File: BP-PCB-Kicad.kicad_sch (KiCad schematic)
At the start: 18 parts, among them J1 A3C-50DA-2DSA_71_, J13 Conn_01x20, J14 Conn_01x20, J15 DF14-30P-1.25H_35_, J16 A3C-50DA-2DSA_71_, J17 A3C-4DA-2DSA_71_, J18 A3C-4DA-2DSA_71_, J19 Molex 55460-0272, J2 A3C-50DA-2DSA_71_, J21 Molex 55460-0272, J22 Molex 55460-0272, J23 DF14-15P-1.25H52, J3 A3C-4DA-2DSA_71_, J4 A3C-4DA-2DSA_71_, J5 A3C-50DA-2DSA_71_, J6 A3C-50DA-2DSA_71_, J7 DF14-15P-1.25H52, J8 DF14-15P-1.25H52

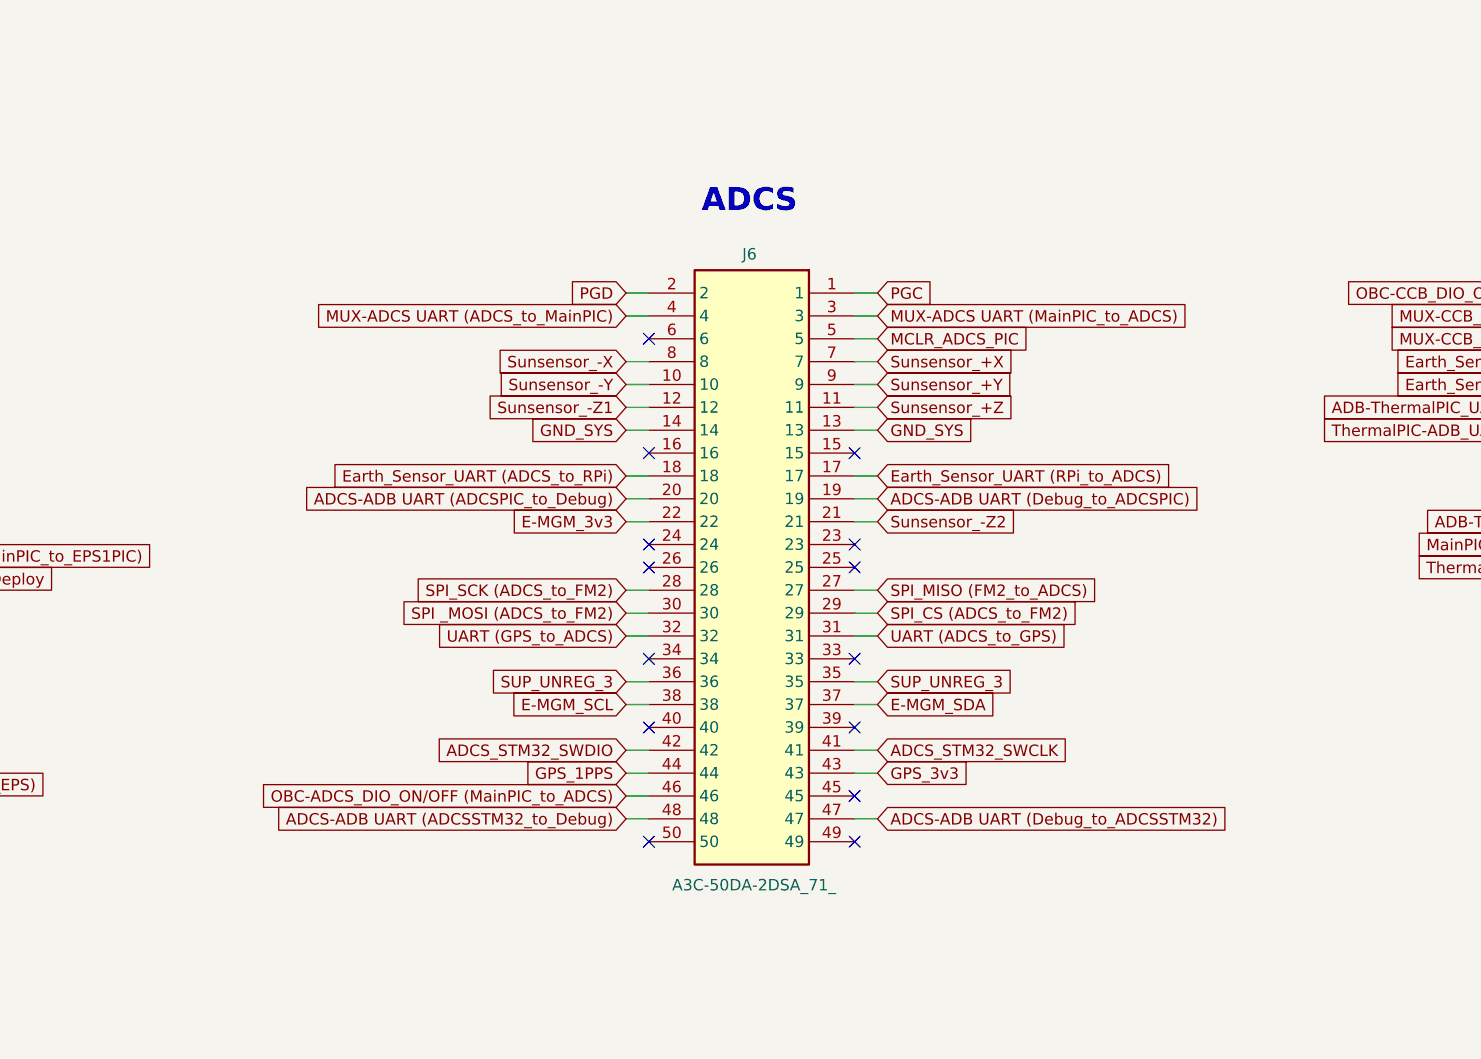
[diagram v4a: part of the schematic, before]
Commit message: Routing traces of panels
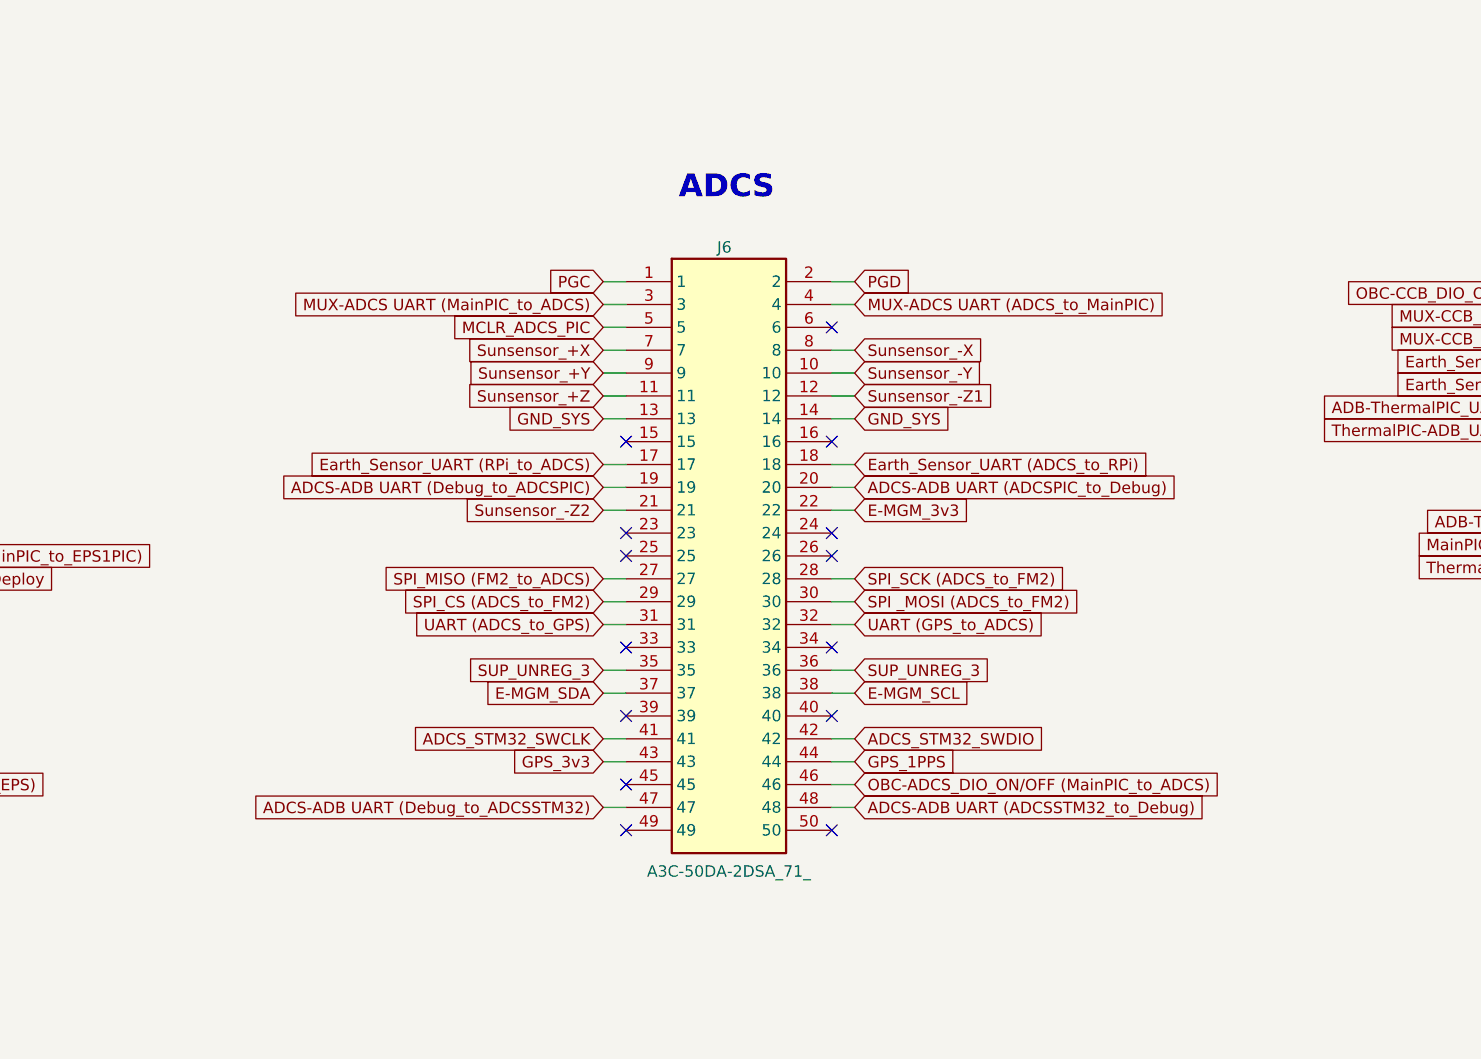
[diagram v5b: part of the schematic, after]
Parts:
- removed J6: A3C-50DA-2DSA_71_, Custom-Footprints:Hirose_A3C-50DA-2DSC(71)_Mirrored, symbol Custom-Symbols:A3C-50DA-2DSA_71_Mirrored
- added J6: A3C-50DA-2DSA_71_, Custom-Footprints:Hirose_A3C-50DA-2DSC(71), symbol Custom-Symbols:A3C-50DA-2DSA_71_
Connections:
- net ADCS-ADB UART (ADCSPIC_to_Debug): now also J6.20
- net ADCS-ADB UART (ADCSSTM32_to_Debug): now also J6.48
- net ADCS-ADB UART (Debug_to_ADCSPIC): now also J6.19
- net ADCS-ADB UART (Debug_to_ADCSSTM32): now also J6.47
- net ADCS_STM32_SWCLK: now also J6.41
- net ADCS_STM32_SWDIO: now also J6.42
- net E-MGM_3v3: now also J6.22
- net E-MGM_SCL: now also J6.38
- net E-MGM_SDA: now also J6.37
- net Earth_Sensor_UART (ADCS_to_RPi): now also J6.18
- net Earth_Sensor_UART (RPi_to_ADCS): now also J6.17
- net GND_SYS: now also J6.13, J6.14
- net GPS_1PPS: now also J6.44
- net GPS_3v3: now also J6.43
- net MCLR_ADCS_PIC: now also J6.5
- net MUX-ADCS UART (ADCS_to_MainPIC): now also J6.4
- net MUX-ADCS UART (MainPIC_to_ADCS): now also J6.3
- net OBC-ADCS_DIO_ON/OFF (MainPIC_to_ADCS): now also J6.46
- net PGC: now also J6.1
- net PGD: now also J6.2
- net SPI _MOSI (ADCS_to_FM2): now also J6.30
- net SPI_CS (ADCS_to_FM2): now also J6.29
- net SPI_MISO (FM2_to_ADCS): now also J6.27
- net SPI_SCK (ADCS_to_FM2): now also J6.28
- net SUP_UNREG_3: now also J6.35, J6.36
- net Sunsensor_+X: now also J6.7
- net Sunsensor_+Y: now also J6.9
- net Sunsensor_+Z: now also J6.11
- net Sunsensor_-X: now also J6.8
- net Sunsensor_-Y: now also J6.10
- net Sunsensor_-Z1: now also J6.12
- net Sunsensor_-Z2: now also J6.21
- net UART (ADCS_to_GPS): now also J6.31
- net UART (GPS_to_ADCS): now also J6.32

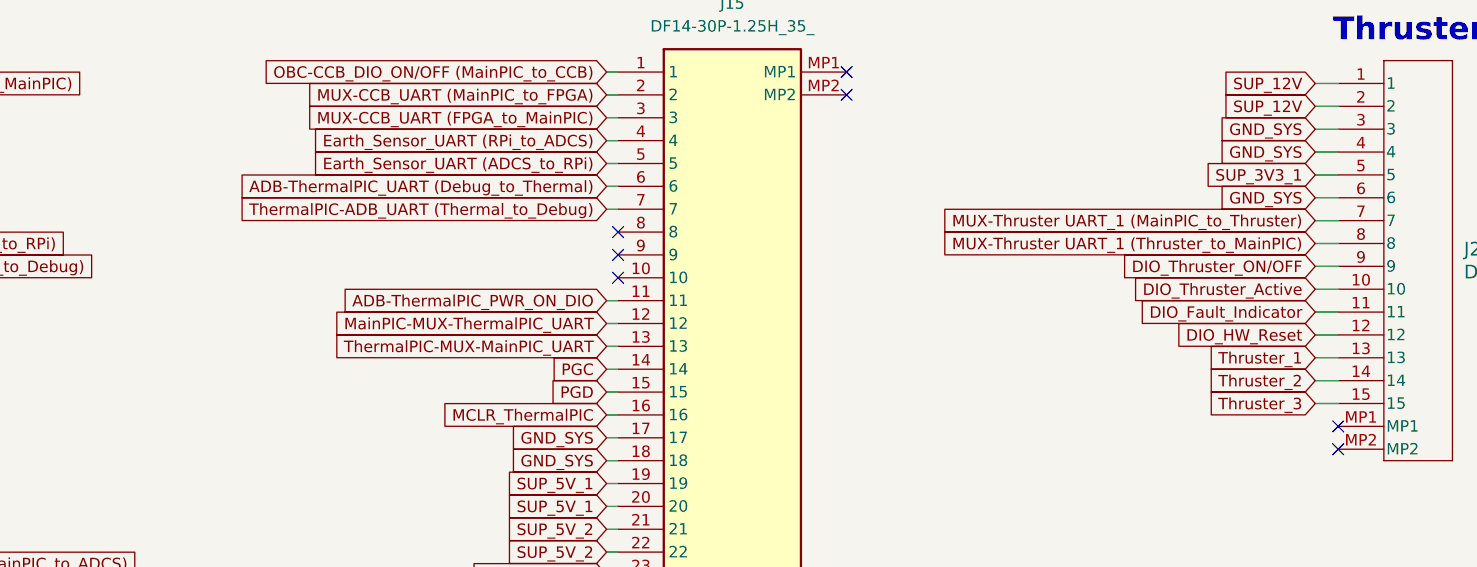
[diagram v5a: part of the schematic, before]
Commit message: Corrected OCP values in schematic and fixed PCB layout
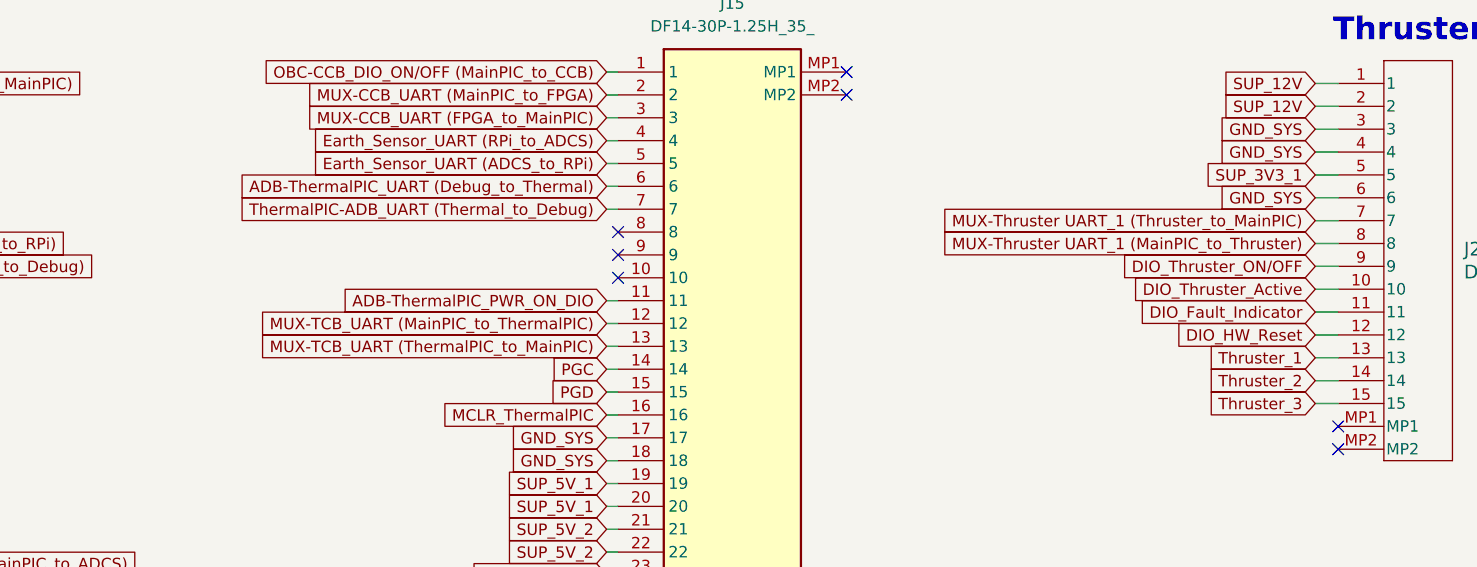
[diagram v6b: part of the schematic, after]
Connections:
- net MUX-Thruster UART_1 (MainPIC_to_Thruster): now also J23.8; no longer J23.7
- net MUX-Thruster UART_1 (Thruster_to_MainPIC): now also J23.7; no longer J23.8
- net MainPIC-MUX-ThermalPIC_UART renamed MUX-TCB_UART (MainPIC_to_ThermalPIC)
- net ThermalPIC-MUX-MainPIC_UART  renamed MUX-TCB_UART (ThermalPIC_to_MainPIC)
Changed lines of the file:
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@@
 	(wire
 		(pts
+			(xy 367.03 157.48) (xy 369.57 157.48)
+		)
+		(stroke
+			(width 0)
+			(type default)
+		)
+	)
+	(wire
+		(pts
 			(xy 278.13 262.89) (xy 279.4 262.89)
 		)
@@
 	(wire
 		(pts
-			(xy 367.03 157.48) (xy 369.57 157.48)
-		)
-		(stroke
-			(width 0)
-			(type default)
-		)
-	)
-	(wire
-		(pts
 			(xy 81.28 200.66) (xy 78.74 200.66)
 		)
@@
 	(wire
 		(pts
-			(xy 367.03 154.94) (xy 369.57 154.94)
+			(xy 300.99 69.85) (xy 303.53 69.85)
 		)
 		(stroke
@@
 	(wire
 		(pts
-			(xy 300.99 69.85) (xy 303.53 69.85)
+			(xy 67.31 237.49) (xy 69.85 237.49)
 		)
 		(stroke
@@
 	(wire
 		(pts
-			(xy 67.31 237.49) (xy 69.85 237.49)
+			(xy 367.03 154.94) (xy 369.57 154.94)
 		)
 		(stroke
@@
 	(global_label "MUX-Thruster UART_1 (MainPIC_to_Thruster)"
 		(shape input)
-		(at 367.03 154.94 180)
+		(at 367.03 157.48 180)
 		(fields_autoplaced yes)
 		(effects
@@
 		)
 		(property "Intersheetrefs" "${INTERSHEET_REFS}"
-			(at 321.3489 154.94 0)
+			(at 321.3489 157.48 0)
 			(effects
 				(font
@@
 		)
 	)
-	(global_label "ThermalPIC-MUX-MainPIC_UART "
+	(global_label "MUX-TCB_UART (ThermalPIC_to_MainPIC)"
 		(shape input)
 		(at 288.29 168.91 180)
@@
 		)
 		(property "Intersheetrefs" "${INTERSHEET_REFS}"
-			(at 253.434 168.91 0)
+			(at 245.9955 168.91 0)
 			(effects
 				(font
@@
 	(global_label "MUX-Thruster UART_1 (Thruster_to_MainPIC)"
 		(shape input)
-		(at 367.03 157.48 180)
+		(at 367.03 154.94 180)
 		(fields_autoplaced yes)
 		(effects
@@
 		)
 		(property "Intersheetrefs" "${INTERSHEET_REFS}"
-			(at 321.3489 157.48 0)
+			(at 321.3489 154.94 0)
 			(effects
 				(font
@@
 		)
 	)
-	(global_label "MainPIC-MUX-ThermalPIC_UART"
+	(global_label "MUX-TCB_UART (MainPIC_to_ThermalPIC)"
 		(shape input)
 		(at 288.29 166.37 180)
@@
 		)
 		(property "Intersheetrefs" "${INTERSHEET_REFS}"
-			(at 254.4016 166.37 0)
+			(at 245.9955 166.37 0)
 			(effects
 				(font
